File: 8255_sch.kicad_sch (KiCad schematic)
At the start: 13 parts, among them U2 8255, U5 8255, U6 8255

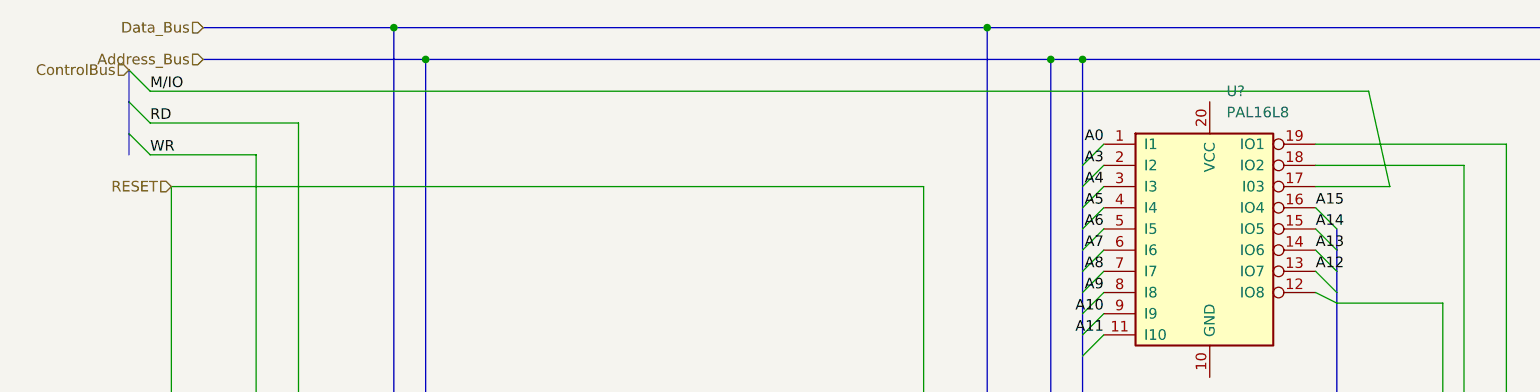
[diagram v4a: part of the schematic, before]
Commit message: Fixed some wires
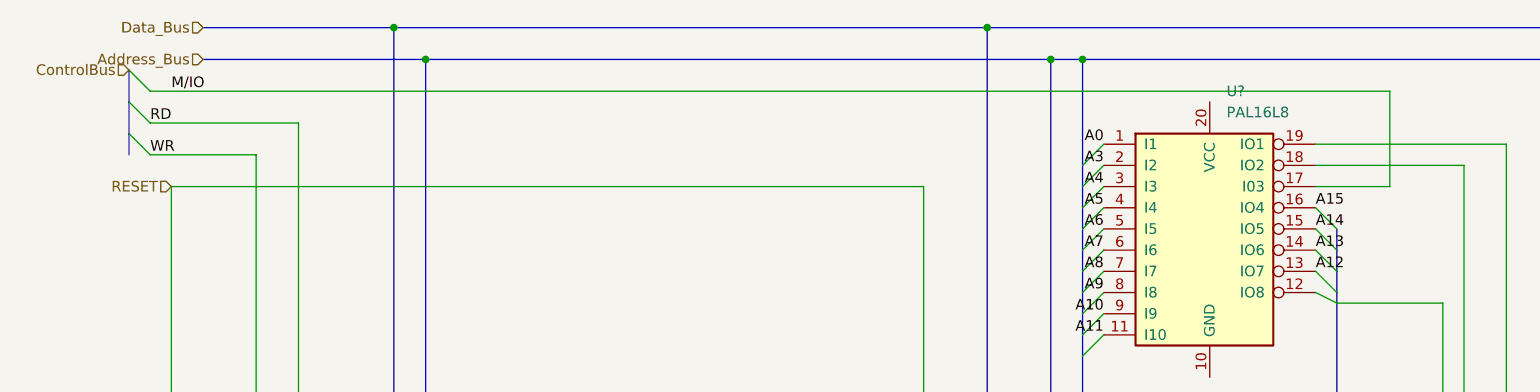
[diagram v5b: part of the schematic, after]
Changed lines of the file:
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@@
   (junction (at 38.1 78.74) (diameter 0) (color 0 0 0 0)
   )
+  (bus_entry (at 17.78 21.59) (size 2.54 2.54)
+    (stroke (width 0) (type default) (color 0 0 0 0))
+  )
   (bus_entry (at 49.53 124.46) (size 2.54 -2.54)
     (stroke (width 0) (type default) (color 0 0 0 0))
@@
     (stroke (width 0) (type default) (color 0 0 0 0))
   )
-  (bus_entry (at 17.78 21.59) (size 2.54 2.54)
-    (stroke (width 0) (type default) (color 0 0 0 0))
-  )
   (bus_entry (at 128.27 114.3) (size 2.54 -2.54)
     (stroke (width 0) (type default) (color 0 0 0 0))
@@
     (stroke (width 0) (type default) (color 0 0 0 0))
   )
-  (wire (pts (xy 20.32 24.13) (xy 166.37 24.13))
+  (wire (pts (xy 20.32 24.13) (xy 168.91 24.13))
     (stroke (width 0) (type default) (color 0 0 0 0))
   )
@@
     (stroke (width 0) (type default) (color 0 0 0 0))
   )
-  (wire (pts (xy 166.37 24.13) (xy 168.91 35.56))
+  (wire (pts (xy 168.91 24.13) (xy 168.91 35.56))
     (stroke (width 0) (type default) (color 0 0 0 0))
   )
@@
     (stroke (width 0) (type default) (color 0 0 0 0))
   )
+  (bus (pts (xy 17.78 25.4) (xy 17.78 29.21))
+    (stroke (width 0) (type default) (color 0 0 0 0))
+  )
   (wire (pts (xy 91.44 154.94) (xy 99.06 154.94))
     (stroke (width 0) (type default) (color 0 0 0 0))
@@
     (stroke (width 0) (type default) (color 0 0 0 0))
   )
+  (wire (pts (xy 175.26 73.66) (xy 175.26 49.53))
+    (stroke (width 0) (type default) (color 0 0 0 0))
+  )
+  (wire (pts (xy 241.3 107.95) (xy 248.92 107.95))
+    (stroke (width 0) (type default) (color 0 0 0 0))
+  )
+  (wire (pts (xy 198.12 128.27) (xy 205.74 128.27))
+    (stroke (width 0) (type default) (color 0 0 0 0))
+  )
+  (wire (pts (xy 91.44 132.08) (xy 99.06 132.08))
+    (stroke (width 0) (type default) (color 0 0 0 0))
+  )
+  (wire (pts (xy 168.91 132.08) (xy 176.53 132.08))
+    (stroke (width 0) (type default) (color 0 0 0 0))
+  )
+  (bus (pts (xy 17.78 29.21) (xy 17.78 31.75))
+    (stroke (width 0) (type default) (color 0 0 0 0))
+  )
+  (wire (pts (xy 91.44 121.92) (xy 99.06 121.92))
+    (stroke (width 0) (type default) (color 0 0 0 0))
+  )
+  (wire (pts (xy 91.44 101.6) (xy 99.06 101.6))
+    (stroke (width 0) (type default) (color 0 0 0 0))
+  )
+  (wire (pts (xy 187.96 71.12) (xy 187.96 105.41))
+    (stroke (width 0) (type default) (color 0 0 0 0))
+  )
+  (wire (pts (xy 187.96 105.41) (xy 205.74 105.41))
+    (stroke (width 0) (type default) (color 0 0 0 0))
+  )
+  (bus (pts (xy 53.34 20.32) (xy 53.34 114.3))
+    (stroke (width 0) (type default) (color 0 0 0 0))
+  )
+  (bus (pts (xy 132.08 48.26) (xy 132.08 50.8))
+    (stroke (width 0) (type default) (color 0 0 0 0))
+  )
   (bus (pts (xy 17.78 21.59) (xy 17.78 25.4))
     (stroke (width 0) (type default) (color 0 0 0 0))
   )
-  (wire (pts (xy 175.26 73.66) (xy 175.26 49.53))
-    (stroke (width 0) (type default) (color 0 0 0 0))
-  )
-  (wire (pts (xy 241.3 107.95) (xy 248.92 107.95))
-    (stroke (width 0) (type default) (color 0 0 0 0))
-  )
-  (wire (pts (xy 198.12 128.27) (xy 205.74 128.27))
-    (stroke (width 0) (type default) (color 0 0 0 0))
-  )
-  (wire (pts (xy 91.44 132.08) (xy 99.06 132.08))
-    (stroke (width 0) (type default) (color 0 0 0 0))
-  )
-  (wire (pts (xy 168.91 132.08) (xy 176.53 132.08))
-    (stroke (width 0) (type default) (color 0 0 0 0))
-  )
-  (bus (pts (xy 17.78 29.21) (xy 17.78 31.75))
-    (stroke (width 0) (type default) (color 0 0 0 0))
-  )
-  (wire (pts (xy 91.44 121.92) (xy 99.06 121.92))
-    (stroke (width 0) (type default) (color 0 0 0 0))
-  )
-  (wire (pts (xy 91.44 101.6) (xy 99.06 101.6))
-    (stroke (width 0) (type default) (color 0 0 0 0))
-  )
-  (wire (pts (xy 187.96 71.12) (xy 187.96 105.41))
-    (stroke (width 0) (type default) (color 0 0 0 0))
-  )
-  (wire (pts (xy 187.96 105.41) (xy 205.74 105.41))
-    (stroke (width 0) (type default) (color 0 0 0 0))
-  )
-  (bus (pts (xy 53.34 20.32) (xy 53.34 114.3))
-    (stroke (width 0) (type default) (color 0 0 0 0))
-  )
-  (bus (pts (xy 132.08 48.26) (xy 132.08 50.8))
-    (stroke (width 0) (type default) (color 0 0 0 0))
-  )
   (wire (pts (xy 185.42 102.87) (xy 205.74 102.87))
     (stroke (width 0) (type default) (color 0 0 0 0))
@@
   )
   (wire (pts (xy 168.91 124.46) (xy 176.53 124.46))
-    (stroke (width 0) (type default) (color 0 0 0 0))
-  )
-  (bus (pts (xy 17.78 25.4) (xy 17.78 29.21))
     (stroke (width 0) (type default) (color 0 0 0 0))
   )
@@
     (effects (font (size 1.27 1.27)) (justify right bottom))
   )
-  (label "M{slash}IO" (at 20.32 24.13 0)
+  (label "M{slash}IO" (at 22.86 24.13 0)
     (effects (font (size 1.27 1.27)) (justify left bottom))
   )

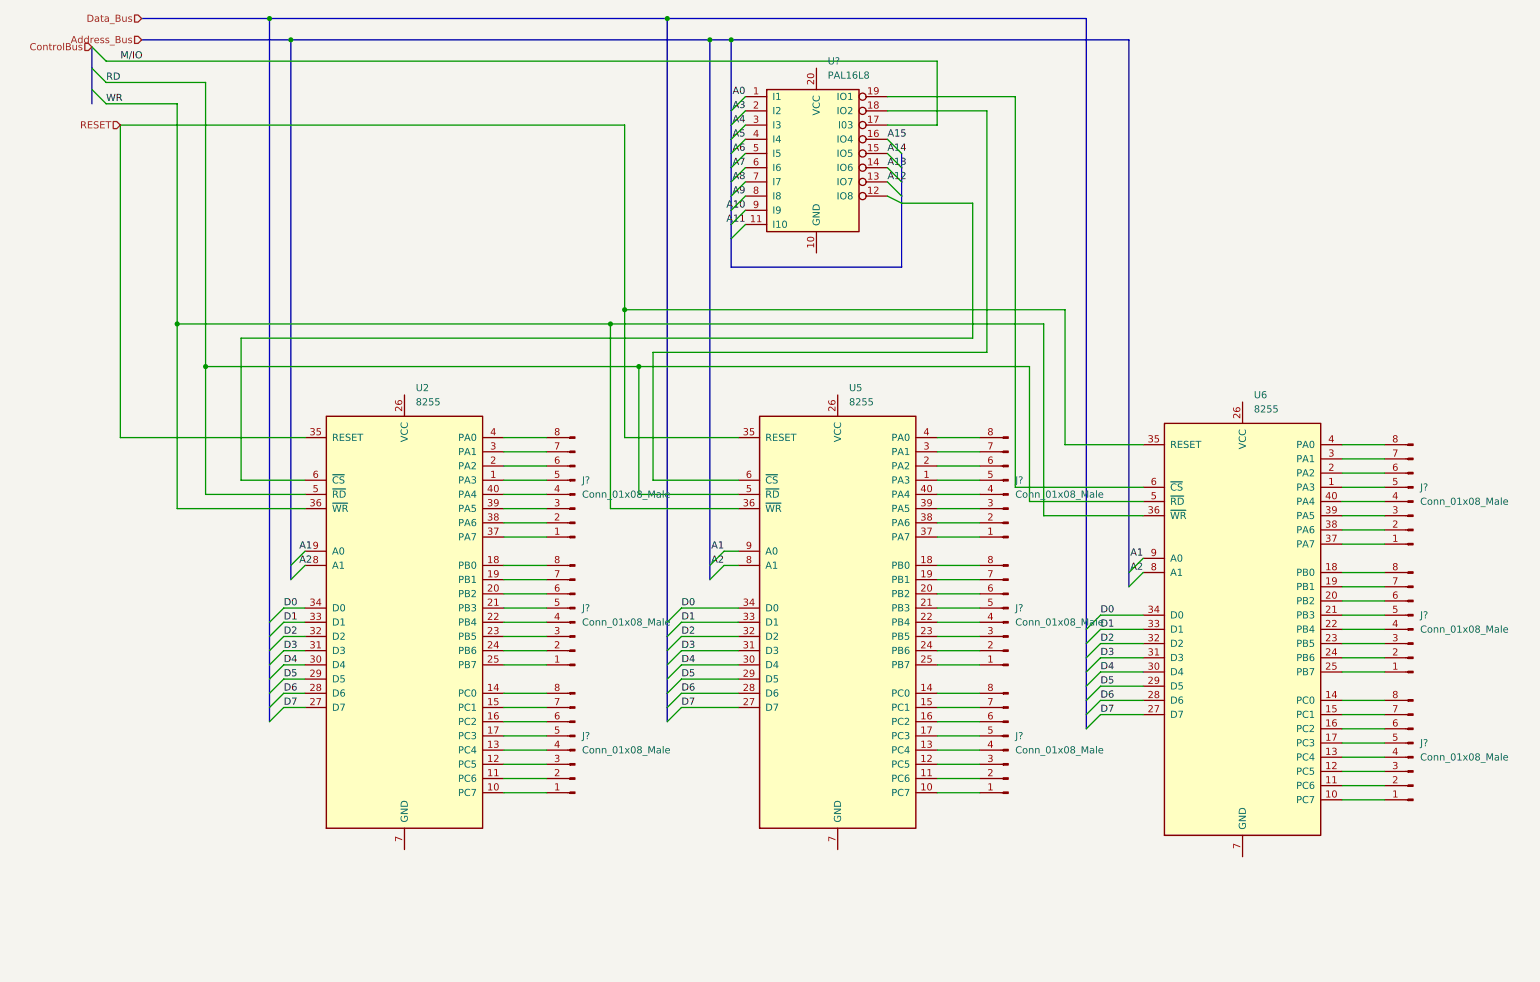
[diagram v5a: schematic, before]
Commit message: Wired Push Buttons and added footprints
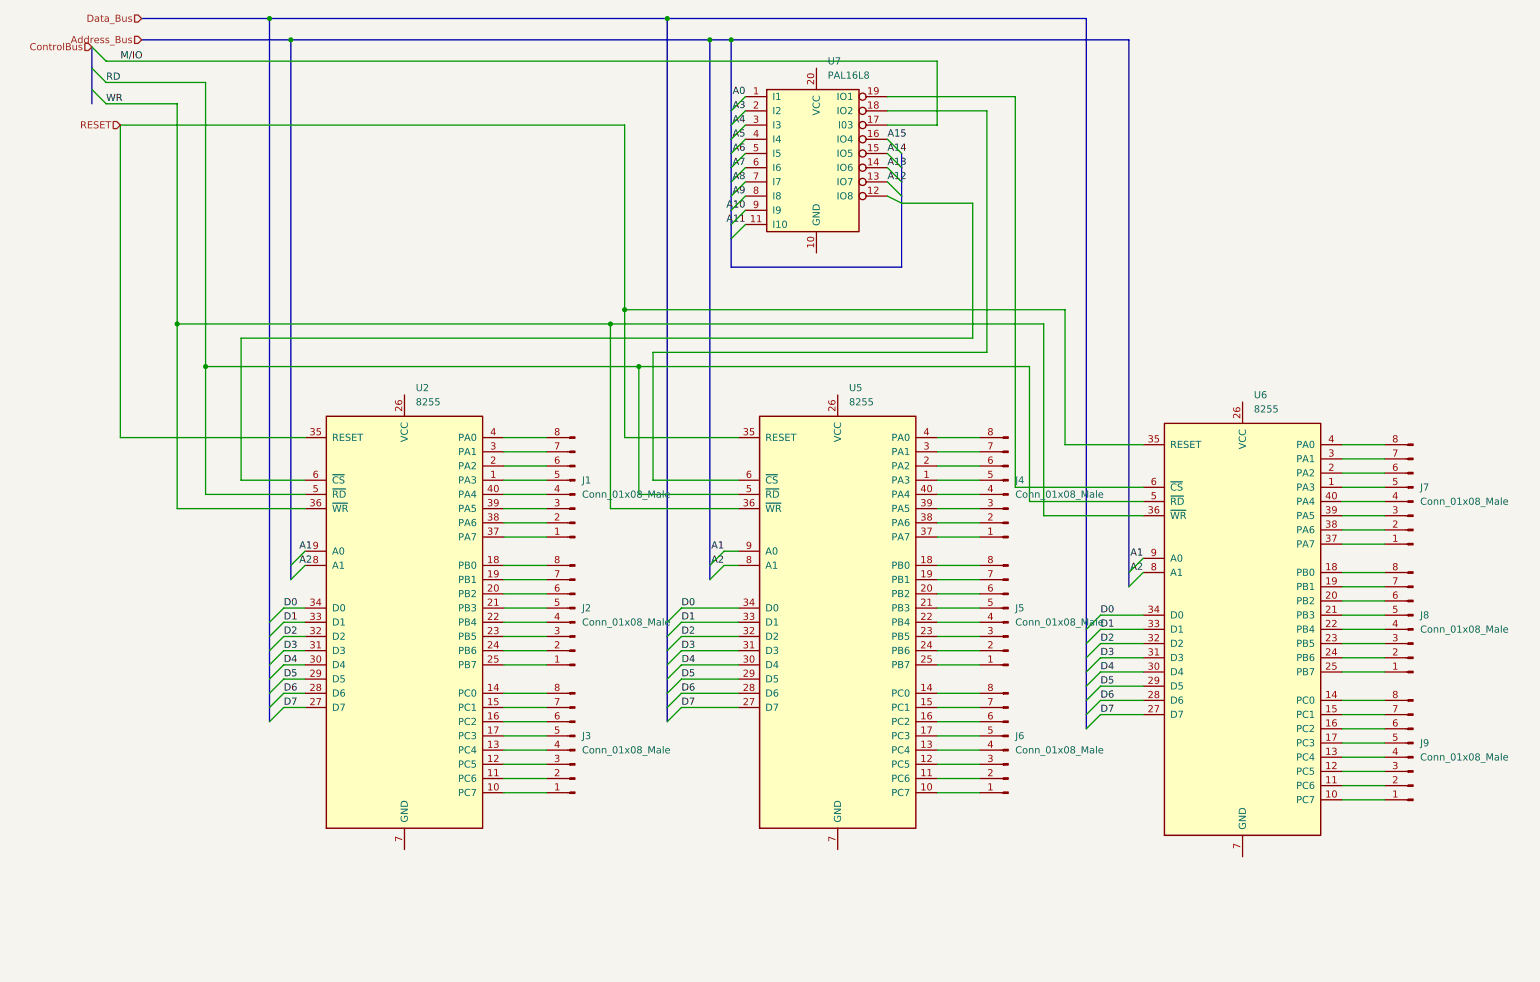
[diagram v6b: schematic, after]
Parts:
- gave numbers to parts that had none: 10
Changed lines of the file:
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@@
   (symbol (lib_id "Logic_Programmable:PAL16L8") (at 147.32 43.18 0) (unit 1)
     (in_bom yes) (on_board yes) (fields_autoplaced)
-    (property "Reference" "U?" (id 0) (at 149.3394 24.13 0)
+    (property "Reference" "U7" (id 0) (at 149.3394 24.13 0)
       (effects (font (size 1.27 1.27)) (justify left))
     )
@@
   (symbol (lib_id "Connector:Conn_01x08_Male") (at 254 125.73 180) (unit 1)
     (in_bom yes) (on_board yes) (fields_autoplaced)
-    (property "Reference" "J?" (id 0) (at 255.27 123.1899 0)
+    (property "Reference" "J8" (id 0) (at 255.27 123.1899 0)
       (effects (font (size 1.27 1.27)) (justify right))
     )
@@
   (symbol (lib_id "Connector:Conn_01x08_Male") (at 181.61 124.46 180) (unit 1)
     (in_bom yes) (on_board yes) (fields_autoplaced)
-    (property "Reference" "J?" (id 0) (at 182.88 121.9199 0)
+    (property "Reference" "J5" (id 0) (at 182.88 121.9199 0)
       (effects (font (size 1.27 1.27)) (justify right))
     )
@@
   (symbol (lib_id "Connector:Conn_01x08_Male") (at 104.14 101.6 180) (unit 1)
     (in_bom yes) (on_board yes) (fields_autoplaced)
-    (property "Reference" "J?" (id 0) (at 105.41 99.0599 0)
+    (property "Reference" "J1" (id 0) (at 105.41 99.0599 0)
       (effects (font (size 1.27 1.27)) (justify right))
     )
@@
   (symbol (lib_id "Connector:Conn_01x08_Male") (at 104.14 124.46 180) (unit 1)
     (in_bom yes) (on_board yes) (fields_autoplaced)
-    (property "Reference" "J?" (id 0) (at 105.41 121.9199 0)
+    (property "Reference" "J2" (id 0) (at 105.41 121.9199 0)
       (effects (font (size 1.27 1.27)) (justify right))
     )
@@
   (symbol (lib_id "Connector:Conn_01x08_Male") (at 181.61 101.6 180) (unit 1)
     (in_bom yes) (on_board yes) (fields_autoplaced)
-    (property "Reference" "J?" (id 0) (at 182.88 99.0599 0)
+    (property "Reference" "J4" (id 0) (at 182.88 99.0599 0)
       (effects (font (size 1.27 1.27)) (justify right))
     )
@@
   (symbol (lib_id "Connector:Conn_01x08_Male") (at 104.14 147.32 180) (unit 1)
     (in_bom yes) (on_board yes) (fields_autoplaced)
-    (property "Reference" "J?" (id 0) (at 105.41 144.7799 0)
+    (property "Reference" "J3" (id 0) (at 105.41 144.7799 0)
       (effects (font (size 1.27 1.27)) (justify right))
     )
@@
   (symbol (lib_id "Connector:Conn_01x08_Male") (at 181.61 147.32 180) (unit 1)
     (in_bom yes) (on_board yes) (fields_autoplaced)
-    (property "Reference" "J?" (id 0) (at 182.88 144.7799 0)
+    (property "Reference" "J6" (id 0) (at 182.88 144.7799 0)
       (effects (font (size 1.27 1.27)) (justify right))
     )
@@
   (symbol (lib_id "Connector:Conn_01x08_Male") (at 254 148.59 180) (unit 1)
     (in_bom yes) (on_board yes) (fields_autoplaced)
-    (property "Reference" "J?" (id 0) (at 255.27 146.0499 0)
+    (property "Reference" "J9" (id 0) (at 255.27 146.0499 0)
       (effects (font (size 1.27 1.27)) (justify right))
     )
@@
   (symbol (lib_id "Connector:Conn_01x08_Male") (at 254 102.87 180) (unit 1)
     (in_bom yes) (on_board yes) (fields_autoplaced)
-    (property "Reference" "J?" (id 0) (at 255.27 100.3299 0)
-      (effects (font (size 1.27 1.27)) (justify right))
-    )
+    (property "Reference" "J7" (id 0) (at 255.27 100.3299 0)
+      (effects (font (size 1.27 1.27)) (justify right))
+    )

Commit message: Added power and ground to chips
Added power and ground to chips as well as checked and added all labels for pins off of busses
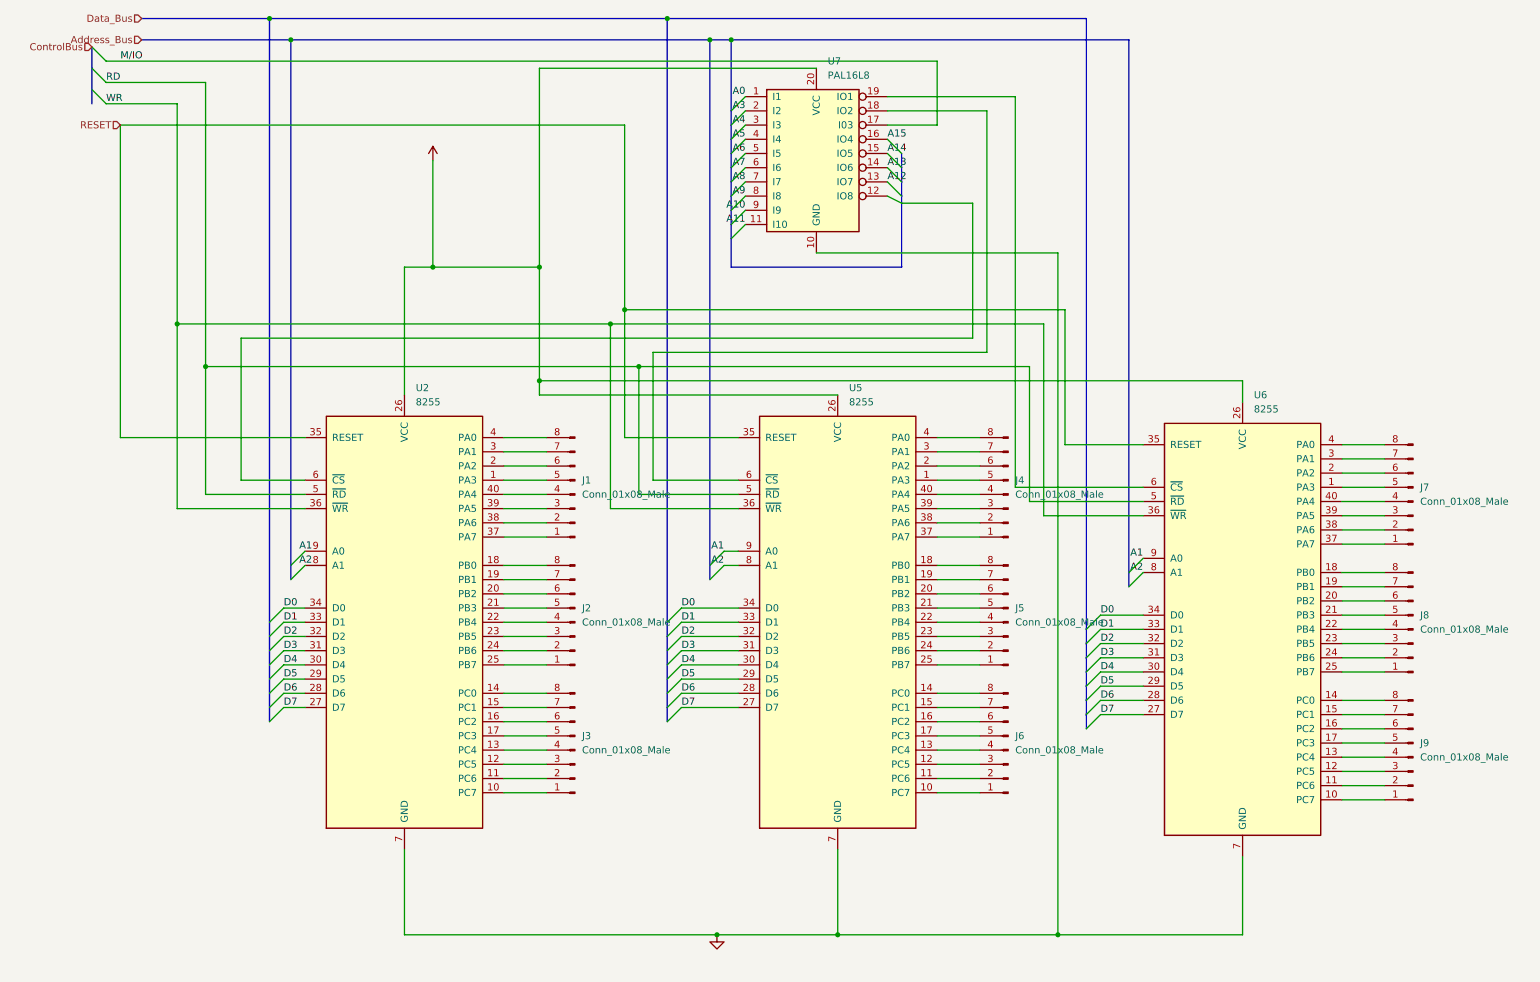
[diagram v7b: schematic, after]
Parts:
- J1, J2, J3, J4, J5, J6, J7, J8, J9: footprint (none) -> Connector_Harwin:Harwin_M20-89008xx_1x08_P2.54mm_Horizontal
- U7: footprint (none) -> Package_DIP:DIP-20_W7.62mm
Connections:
- net +5V: now reaches U2.26 (VCC)
- net +5V: now also U5.26 (VCC), U6.26 (VCC), U7.20 (VCC)
- net GND: now reaches U2.7 (GND)
- net GND: now also U5.7 (GND), U6.7 (GND), U7.10 (GND)
